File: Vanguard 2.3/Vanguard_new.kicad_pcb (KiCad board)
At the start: 4 copper layers, 42.1 x 51.9 mm, 86 parts, among them J1 USB_C_Receptacle_USB2.0_16P, J2 Conn_02x03_Pin, J3 Micro_SD_Card_Det1, J4 STARBOARD_SERVO, J5 PORTSIDE_SERVO, J6 Battery In, J7 EJECTION_SERVO, Q1 BSS138, Q2 BSS138, Q3 BSS138, Q4 BSS138, U1 ATSAMD11D14A-M, U2 ATmega4809-A, U3 AT25DF641A-SH-T, U4 AP2112K-3.3, U5 BD1020HFV, U6 BNO086, U7 TXB0104D, U8 TPS61092, U9 MPM3610AGQV-P, Y1 32.768kHz

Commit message: closed kicad
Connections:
- C4 pad 1: Net-(U9-IN) -> BATT_IN
- J1 pad S1: unconnected-(J1-SHIELD-PadS1) -> GND
- R14 pad 1: Net-(U9-IN) -> BATT_IN
- U9 pad 16: Net-(U9-IN) -> BATT_IN
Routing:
- net unconnected-(J1-SHIELD-PadS1): track 22.9 -> 0.00 mm, vias 2 -> 0
- net GND: track 80.1 -> 82.9 mm, vias 41 -> 42
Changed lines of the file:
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@@
 	(net 125 "Net-(BZ1-+)")
 	(net 126 "Net-(D7-A)")
-	(net 127 "Net-(U9-IN)")
-	(net 128 "unconnected-(J1-SHIELD-PadS1)")
 	(footprint "Jumper:SolderJumper-2_P1.3mm_Bridged2Bar_Pad1.0x1.5mm"
 		(layer "F.Cu")
@@
 			(layers "F.Cu" "F.Paste" "F.Mask")
 			(roundrect_rratio 0.25)
-			(net 127 "Net-(U9-IN)")
+			(net 3 "BATT_IN")
 			(pinfunction "IN")
 			(pintype "input")
@@
 			(layers "*.Cu" "*.Mask")
 			(remove_unused_layers no)
-			(net 128 "unconnected-(J1-SHIELD-PadS1)")
+			(net 2 "GND")
 			(pinfunction "SHIELD")
 			(pintype "passive")
@@
 			(layers "*.Cu" "*.Mask")
 			(remove_unused_layers no)
-			(net 128 "unconnected-(J1-SHIELD-PadS1)")
+			(net 2 "GND")
 			(pinfunction "SHIELD")
 			(pintype "passive")
@@
 			(layers "*.Cu" "*.Mask")
 			(remove_unused_layers no)
-			(net 128 "unconnected-(J1-SHIELD-PadS1)")
+			(net 2 "GND")
 			(pinfunction "SHIELD")
 			(pintype "passive")
@@
 			(layers "*.Cu" "*.Mask")
 			(remove_unused_layers no)
-			(net 128 "unconnected-(J1-SHIELD-PadS1)")
+			(net 2 "GND")
 			(pinfunction "SHIELD")
 			(pintype "passive")
@@
 			(layers "F.Cu" "F.Mask")
 			(roundrect_rratio 0.25)
-			(net 127 "Net-(U9-IN)")
+			(net 3 "BATT_IN")
 			(pintype "passive")
 		)
@@
 			(layers "F.Cu" "F.Paste" "F.Mask")
 			(roundrect_rratio 0.25)
-			(net 127 "Net-(U9-IN)")
+			(net 3 "BATT_IN")
 			(pintype "passive")
 		)
@@
 	)
 	(segment
-		(start 118.76 121.62)
-		(end 118.14 121)
+		(start 124.736774 91.04454)
+		(end 124.39546 91.04454)
 		(width 0.2)
 		(layer "F.Cu")
@@
 	)
 	(segment
+		(start 118.14 121.14)
+		(end 119.5 122.5)
+		(width 0.2)
+		(layer "F.Cu")
+		(net 2)
+	)
+	(segment
 		(start 124.502415 106.493668)
 		(end 125.450545 107.441798)
@@
 	)
 	(segment
+		(start 118.14 121)
+		(end 118.14 121.14)
+		(width 0.2)
+		(layer "F.Cu")
+		(net 2)
+	)
+	(segment
 		(start 113.222499 122.155)
 		(end 113.162499 122.095)
@@
 	)
 	(segment
-		(start 118.85 121.62)
-		(end 118.76 121.62)
-		(width 0.2)
-		(layer "F.Cu")
-		(net 2)
-	)
-	(segment
 		(start 127.882784 90.170551)
 		(end 127.842784 90.210551)
@@
 	)
 	(segment
+		(start 125.682785 91.990551)
+		(end 124.736774 91.04454)
+		(width 0.2)
+		(layer "F.Cu")
+		(net 2)
+	)
+	(segment
 		(start 132.95 110.07)
 		(end 132.4 110.07)
@@
 	)
 	(via
+		(at 124.39546 91.04454)
+		(size 0.6)
+		(drill 0.3)
+		(layers "F.Cu" "B.Cu")
+		(net 2)
+	)
+	(via
 		(at 131.79 111.13)
 		(size 0.6)
@@
 	)
 	(via
-		(at 118.85 121.62)
+		(at 119.5 122.5)
 		(size 0.6)
 		(drill 0.3)
@@
 		(net 126)
 	)
-	(segment
-		(start 124.736774 91.04454)
-		(end 124.39546 91.04454)
-		(width 0.2)
-		(layer "F.Cu")
-		(net 128)
-	)
-	(segment
-		(start 128.089449 91.630551)
-		(end 131.632785 91.630551)
-		(width 0.2)
-		(layer "F.Cu")
-		(net 128)
-	)
-	(segment
-		(start 127.630735 92.089265)
-		(end 128.089449 91.630551)
-		(width 0.2)
-		(layer "F.Cu")
-		(net 128)
-	)
-	(segment
-		(start 131.632785 100.610551)
-		(end 131.272785 100.250551)
-		(width 0.2)
-		(layer "F.Cu")
-		(net 128)
-	)
-	(segment
-		(start 131.272785 100.250551)
-		(end 125.682785 100.250551)
-		(width 0.2)
-		(layer "F.Cu")
-		(net 128)
-	)
-	(segment
-		(start 125.682785 91.990551)
-		(end 124.736774 91.04454)
-		(width 0.2)
-		(layer "F.Cu")
-		(net 128)
-	)
-	(via
-		(at 124.39546 91.04454)
-		(size 0.6)
-		(drill 0.3)
-		(layers "F.Cu" "B.Cu")
-		(net 128)
-	)
-	(via
-		(at 127.630735 92.089265)
-		(size 0.6)
-		(drill 0.3)
-		(layers "F.Cu" "B.Cu")
-		(net 128)
-	)
-	(segment
-		(start 125.682785 91.990551)
-		(end 127.532021 91.990551)
-		(width 0.2)
-		(layer "B.Cu")
-		(net 128)
-	)
-	(segment
-		(start 127.532021 91.990551)
-		(end 127.630735 92.089265)
-		(width 0.2)
-		(layer "B.Cu")
-		(net 128)
-	)
-	(segment
-		(start 131.632785 91.630551)
-		(end 131.632785 100.610551)
-		(width 0.2)
-		(layer "B.Cu")
-		(net 128)
-	)
 	(zone

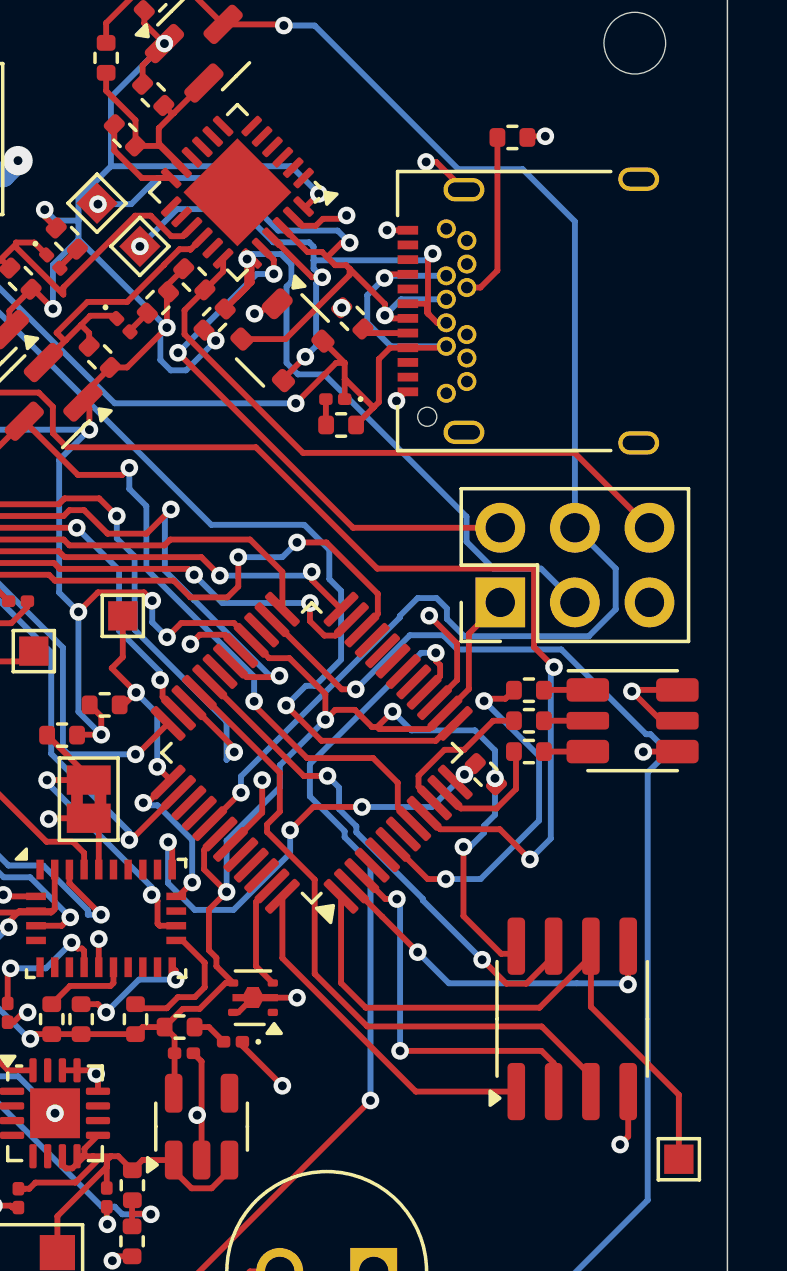
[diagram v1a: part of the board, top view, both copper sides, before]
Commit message: missed gnd wiring
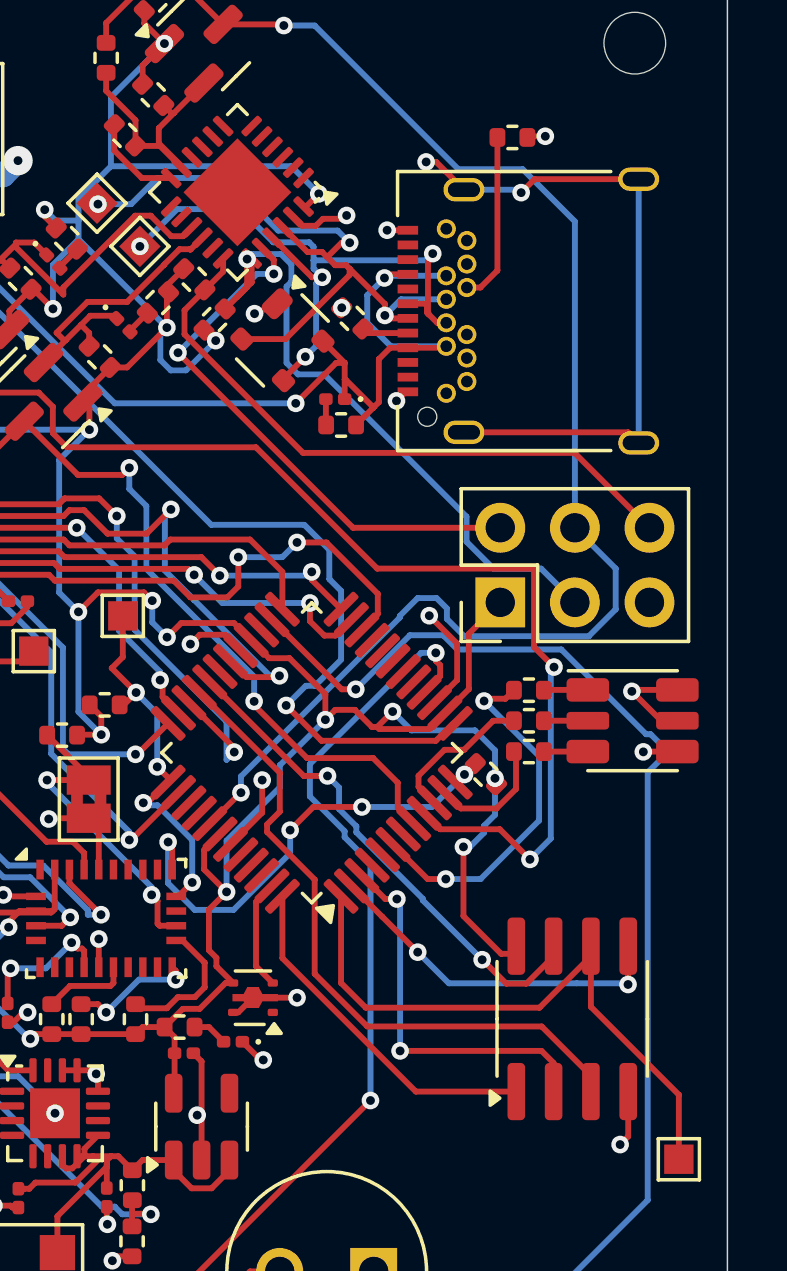
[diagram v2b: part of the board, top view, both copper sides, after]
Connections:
- C4 pad 1: BATT_IN -> Net-(U9-IN)
- J1 pad S1: GND -> unconnected-(J1-SHIELD-PadS1)
- R14 pad 1: BATT_IN -> Net-(U9-IN)
- U9 pad 16: BATT_IN -> Net-(U9-IN)
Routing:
- net unconnected-(J1-SHIELD-PadS1): track 0.00 -> 22.9 mm, vias 0 -> 2
- net GND: track 82.9 -> 80.1 mm, vias 42 -> 41
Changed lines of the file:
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@@
 	(net 125 "Net-(BZ1-+)")
 	(net 126 "Net-(D7-A)")
+	(net 127 "Net-(U9-IN)")
+	(net 128 "unconnected-(J1-SHIELD-PadS1)")
 	(footprint "Jumper:SolderJumper-2_P1.3mm_Bridged2Bar_Pad1.0x1.5mm"
 		(layer "F.Cu")
@@
 			(layers "F.Cu" "F.Paste" "F.Mask")
 			(roundrect_rratio 0.25)
-			(net 3 "BATT_IN")
+			(net 127 "Net-(U9-IN)")
 			(pinfunction "IN")
 			(pintype "input")
@@
 			(layers "*.Cu" "*.Mask")
 			(remove_unused_layers no)
-			(net 2 "GND")
+			(net 128 "unconnected-(J1-SHIELD-PadS1)")
 			(pinfunction "SHIELD")
 			(pintype "passive")
@@
 			(layers "*.Cu" "*.Mask")
 			(remove_unused_layers no)
-			(net 2 "GND")
+			(net 128 "unconnected-(J1-SHIELD-PadS1)")
 			(pinfunction "SHIELD")
 			(pintype "passive")
@@
 			(layers "*.Cu" "*.Mask")
 			(remove_unused_layers no)
-			(net 2 "GND")
+			(net 128 "unconnected-(J1-SHIELD-PadS1)")
 			(pinfunction "SHIELD")
 			(pintype "passive")
@@
 			(layers "*.Cu" "*.Mask")
 			(remove_unused_layers no)
-			(net 2 "GND")
+			(net 128 "unconnected-(J1-SHIELD-PadS1)")
 			(pinfunction "SHIELD")
 			(pintype "passive")
@@
 			(layers "F.Cu" "F.Mask")
 			(roundrect_rratio 0.25)
-			(net 3 "BATT_IN")
+			(net 127 "Net-(U9-IN)")
 			(pintype "passive")
 		)
@@
 			(layers "F.Cu" "F.Paste" "F.Mask")
 			(roundrect_rratio 0.25)
-			(net 3 "BATT_IN")
+			(net 127 "Net-(U9-IN)")
 			(pintype "passive")
 		)
@@
 	)
 	(segment
-		(start 124.736774 91.04454)
-		(end 124.39546 91.04454)
+		(start 118.76 121.62)
+		(end 118.14 121)
 		(width 0.2)
 		(layer "F.Cu")
@@
 	)
 	(segment
-		(start 118.14 121.14)
-		(end 119.5 122.5)
-		(width 0.2)
-		(layer "F.Cu")
-		(net 2)
-	)
-	(segment
 		(start 124.502415 106.493668)
 		(end 125.450545 107.441798)
@@
 	)
 	(segment
-		(start 118.14 121)
-		(end 118.14 121.14)
-		(width 0.2)
-		(layer "F.Cu")
-		(net 2)
-	)
-	(segment
 		(start 113.222499 122.155)
 		(end 113.162499 122.095)
@@
 	)
 	(segment
+		(start 118.85 121.62)
+		(end 118.76 121.62)
+		(width 0.2)
+		(layer "F.Cu")
+		(net 2)
+	)
+	(segment
 		(start 127.882784 90.170551)
 		(end 127.842784 90.210551)
@@
 	)
 	(segment
-		(start 125.682785 91.990551)
-		(end 124.736774 91.04454)
-		(width 0.2)
-		(layer "F.Cu")
-		(net 2)
-	)
-	(segment
 		(start 132.95 110.07)
 		(end 132.4 110.07)
@@
 	)
 	(via
-		(at 124.39546 91.04454)
-		(size 0.6)
-		(drill 0.3)
-		(layers "F.Cu" "B.Cu")
-		(net 2)
-	)
-	(via
 		(at 131.79 111.13)
 		(size 0.6)
@@
 	)
 	(via
-		(at 119.5 122.5)
+		(at 118.85 121.62)
 		(size 0.6)
 		(drill 0.3)
@@
 		(net 126)
 	)
+	(segment
+		(start 124.736774 91.04454)
+		(end 124.39546 91.04454)
+		(width 0.2)
+		(layer "F.Cu")
+		(net 128)
+	)
+	(segment
+		(start 128.089449 91.630551)
+		(end 131.632785 91.630551)
+		(width 0.2)
+		(layer "F.Cu")
+		(net 128)
+	)
+	(segment
+		(start 127.630735 92.089265)
+		(end 128.089449 91.630551)
+		(width 0.2)
+		(layer "F.Cu")
+		(net 128)
+	)
+	(segment
+		(start 131.632785 100.610551)
+		(end 131.272785 100.250551)
+		(width 0.2)
+		(layer "F.Cu")
+		(net 128)
+	)
+	(segment
+		(start 131.272785 100.250551)
+		(end 125.682785 100.250551)
+		(width 0.2)
+		(layer "F.Cu")
+		(net 128)
+	)
+	(segment
+		(start 125.682785 91.990551)
+		(end 124.736774 91.04454)
+		(width 0.2)
+		(layer "F.Cu")
+		(net 128)
+	)
+	(via
+		(at 124.39546 91.04454)
+		(size 0.6)
+		(drill 0.3)
+		(layers "F.Cu" "B.Cu")
+		(net 128)
+	)
+	(via
+		(at 127.630735 92.089265)
+		(size 0.6)
+		(drill 0.3)
+		(layers "F.Cu" "B.Cu")
+		(net 128)
+	)
+	(segment
+		(start 125.682785 91.990551)
+		(end 127.532021 91.990551)
+		(width 0.2)
+		(layer "B.Cu")
+		(net 128)
+	)
+	(segment
+		(start 127.532021 91.990551)
+		(end 127.630735 92.089265)
+		(width 0.2)
+		(layer "B.Cu")
+		(net 128)
+	)
+	(segment
+		(start 131.632785 91.630551)
+		(end 131.632785 100.610551)
+		(width 0.2)
+		(layer "B.Cu")
+		(net 128)
+	)
 	(zone
